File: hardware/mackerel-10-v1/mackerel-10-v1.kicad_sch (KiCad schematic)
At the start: 8 parts, among them J1 Conn_02x05_Odd_Even, U1 68010D, X1 40 MHz

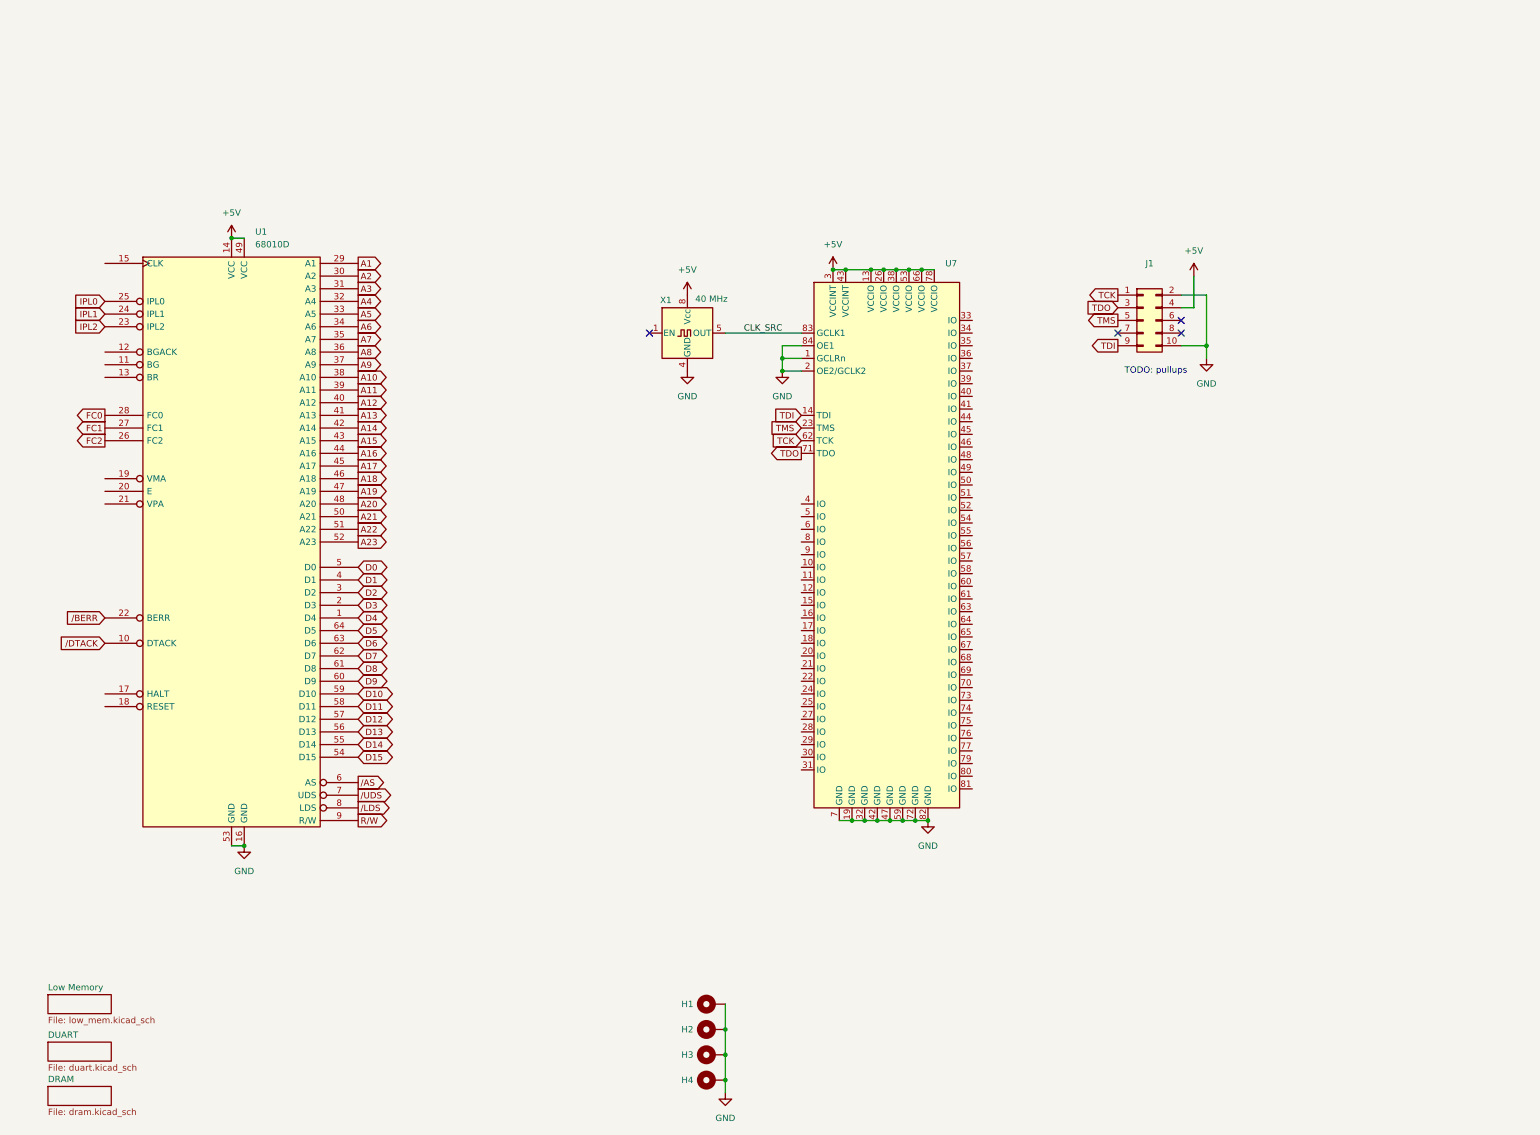
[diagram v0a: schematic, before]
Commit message: Symbol and footprint for SIMM-30 DRAM stubbed out
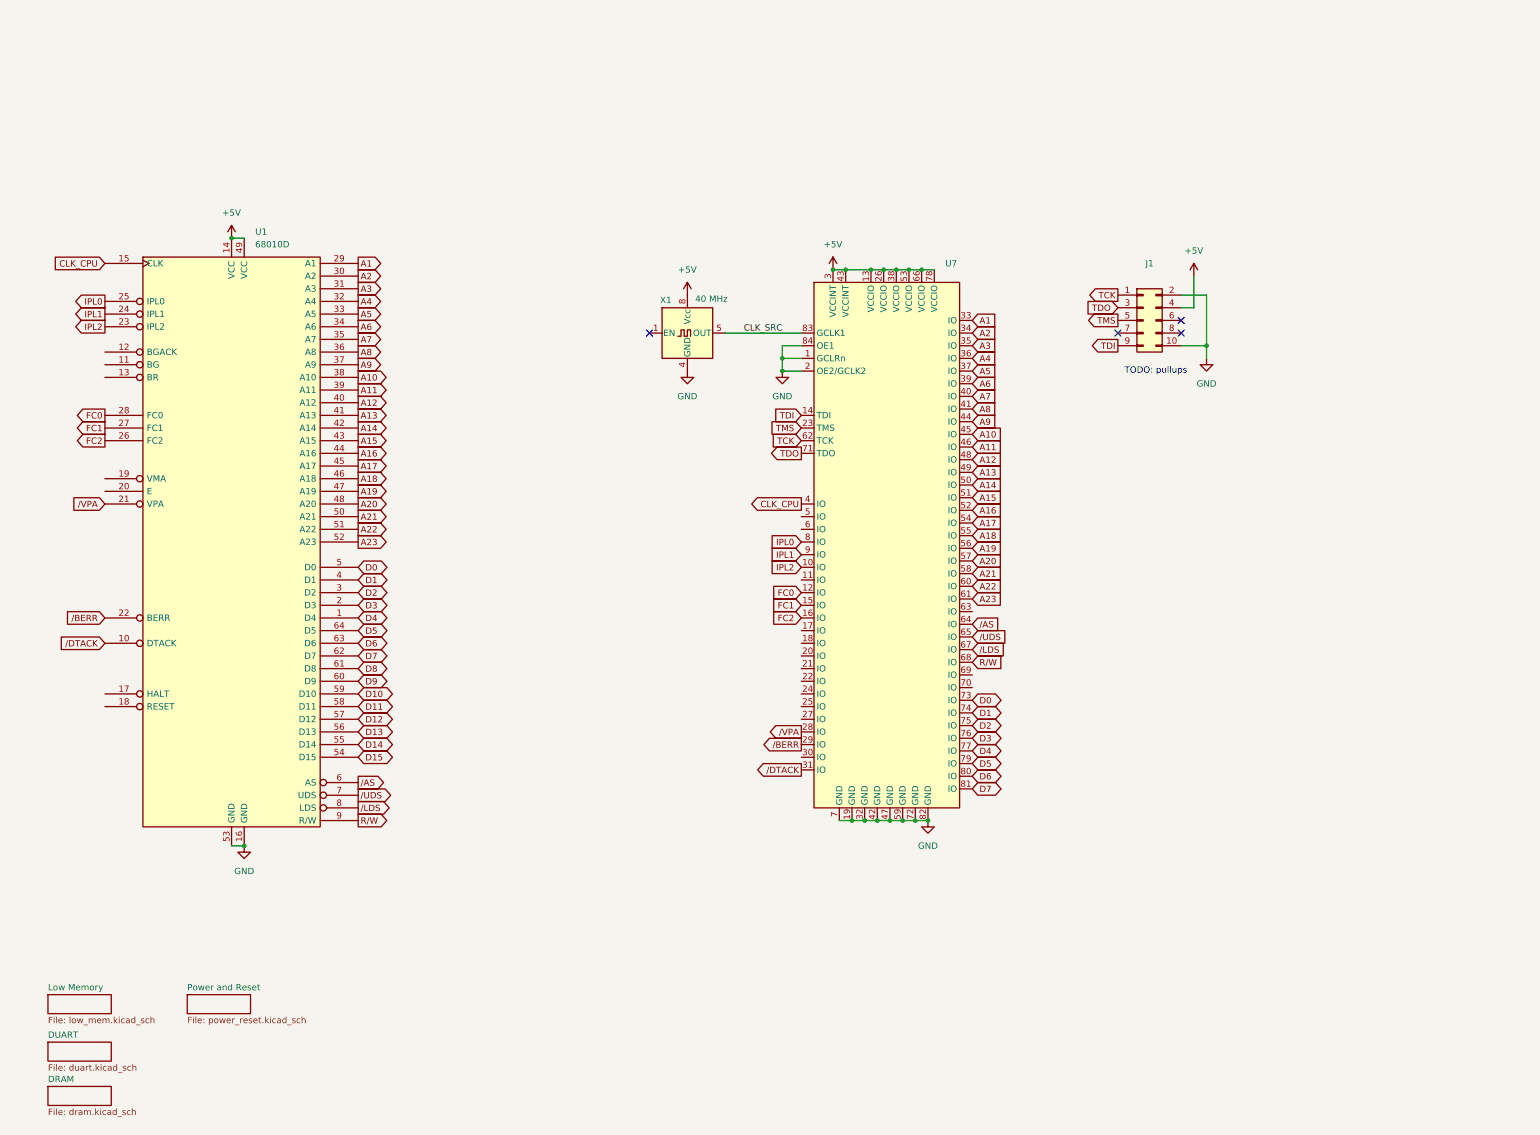
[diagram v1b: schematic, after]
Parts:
- removed H1, H2, H3, H4: MountingHole_Pad, MountingHole:MountingHole_3.2mm_M3_Pad_Via, symbol Mechanical:MountingHole_Pad
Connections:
- net A1: now also U7.33 (IO)
- net A10: now also U7.45 (IO)
- net A11: now also U7.46 (IO)
- net A12: now also U7.48 (IO)
- net A13: now also U7.49 (IO)
- net A14: now also U7.50 (IO)
- net A15: now also U7.51 (IO)
- net A16: now also U7.52 (IO)
- net A17: now also U7.54 (IO)
- net A18: now also U7.55 (IO)
- net A19: now also U7.56 (IO)
- net A2: now also U7.34 (IO)
- net A20: now also U7.57 (IO)
- net A21: now also U7.58 (IO)
- net A22: now also U7.60 (IO)
- net A23: now also U7.61 (IO)
- net A3: now also U7.35 (IO)
- net A4: now also U7.36 (IO)
- net A5: now also U7.37 (IO)
- net A6: now also U7.39 (IO)
- net A7: now also U7.40 (IO)
- net A8: now also U7.41 (IO)
- net A9: now also U7.44 (IO)
- net D0: now also U7.73 (IO)
- net D1: now also U7.74 (IO)
- net D2: now also U7.75 (IO)
- net D3: now also U7.76 (IO)
- net D4: now also U7.77 (IO)
- net D5: now also U7.79 (IO)
- net D6: now also U7.80 (IO)
- net D7: now also U7.81 (IO)
- net FC0: now also U7.12 (IO)
- net FC1: now also U7.15 (IO)
- net FC2: now also U7.16 (IO)
- net IPL0: now also U7.8 (IO)
- net IPL1: now also U7.9 (IO)
- net IPL2: now also U7.10 (IO)
- net R/W: now also U7.68 (IO)
- net /AS: now also U7.64 (IO)
- net /BERR: now also U7.29 (IO)
- net /DTACK: now also U7.31 (IO)
- net /LDS: now also U7.67 (IO)
- net /UDS: now also U7.65 (IO)
- net CLK_CPU: now reaches U1.15 (CLK)
- net CLK_CPU: now also U7.4 (IO)
- net /VPA: now reaches U1.21 (VPA)
- net /VPA: now also U7.28 (IO)
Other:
- added sheet Power and Reset (power_reset.kicad_sch)

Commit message: Trying to figure out Mackerel-10 components
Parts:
- added J2: DIN41612_02x32_AC, Connector_DIN:DIN41612_C_2x32_Male_Horizontal_THT, symbol Connector:DIN41612_02x32_AC
- added R1, R2, R3, R4, R5, R6, R7, R8, R9: R, Resistor_THT:R_Axial_DIN0204_L3.6mm_D1.6mm_P5.08mm_Horizontal, symbol Device:R
- X1: value 40 MHz -> 50 MHz
- renumbered U7 to U2
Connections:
- net +5V: now also R1.1, R2.1, R3.1, R4.1, R5.1, R6.1, R7.1, R8.1
- net A1: no longer U2.33 (IO)
- net A10: no longer U2.45 (IO)
- net A11: no longer U2.46 (IO)
- net A12: no longer U2.48 (IO)
- net A13: no longer U2.49 (IO)
- net A14: no longer U2.50 (IO)
- net A15: no longer U2.51 (IO)
- net A16: now also U2.33 (IO); no longer U2.52 (IO)
- net A17: now also U2.34 (IO); no longer U2.54 (IO)
- net A18: now also U2.35 (IO); no longer U2.55 (IO)
- net A19: now also U2.36 (IO); no longer U2.56 (IO)
- net A2: no longer U2.34 (IO)
- net A20: now also U2.37 (IO); no longer U2.57 (IO)
- net A21: now also U2.39 (IO); no longer U2.58 (IO)
- net A22: now also U2.40 (IO); no longer U2.60 (IO)
- net A23: now also U2.41 (IO); no longer U2.61 (IO)
- net A3: no longer U2.35 (IO)
- net A4: no longer U2.36 (IO)
- net A5: no longer U2.37 (IO)
- net A6: no longer U2.39 (IO)
- net A7: no longer U2.40 (IO)
- net A8: no longer U2.41 (IO)
- net A9: no longer U2.44 (IO)
- net D0: no longer U2.73 (IO)
- net D1: no longer U2.74 (IO)
- net D2: no longer U2.75 (IO)
- net D3: no longer U2.76 (IO)
- net D4: no longer U2.77 (IO)
- net D5: no longer U2.79 (IO)
- net D6: no longer U2.80 (IO)
- net D7: no longer U2.81 (IO)
- net FC0: now also U2.25 (IO); no longer U2.12 (IO)
- net FC1: now also U2.27 (IO); no longer U2.15 (IO)
- net FC2: now also U2.28 (IO); no longer U2.16 (IO)
- net GND: now also R9.2; no longer U2.2 (OE2/GCLK2)
- net IPL0: now also R5.2; no longer U2.8 (IO)
- net IPL1: now also R4.2; no longer U2.9 (IO)
- net IPL2: now also R3.2; no longer U2.10 (IO)
- net R/W: now also U2.77 (IO); no longer U2.68 (IO)
- net TCK: now also R9.1
- net TDI: now also R8.2
- net TDO: now also R6.2
- net TMS: now also R7.2
- net /AS: now also U2.74 (IO); no longer U2.64 (IO)
- net /BERR: now also U2.30 (IO); no longer U2.29 (IO)
- net /LDS: now also U2.76 (IO); no longer U2.67 (IO)
- net /UDS: now also U2.75 (IO); no longer U2.65 (IO)
- net /VPA: now also U2.29 (IO); no longer U2.28 (IO)
- net at U1.12 (BGACK): now also R2.2
- net at U1.13 (BR): now also R1.2
- net /RESET: now reaches U1.17 (HALT)
- net /RESET: now also U1.18 (RESET), U2.5 (IO)
- net /DUART: now reaches U2.11 (IO)
- net /IRQ1: now reaches U2.17 (IO)
- net /IRQ2: now reaches U2.18 (IO)
- net /IRQ3: now reaches U2.20 (IO)
- net /IACK1: now reaches U2.21 (IO)
- net /IACK2: now reaches U2.22 (IO)
- net /IACK3: now reaches U2.24 (IO)
- net /EVENRAM: now reaches U2.6 (IO)
- new net /DTACK_DUART: U2.15 (IO)
- new net /DTACK_EXP: U2.16 (IO)
- new net /EVENROM: U2.9 (IO)
- new net /EXP: U2.12 (IO)
- new net /IPL0: U2.79 (IO)
- new net /IPL1: U2.80 (IO)
- new net /IPL2: U2.81 (IO)
- new net /ODDRAM: U2.8 (IO)
- new net /ODDROM: U2.10 (IO)
- no-connect marks 4 -> 7
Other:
- removed sheet DRAM
- note added: "TODO: IDE lines"
- note added: "TODO: switch to a 44 pin CPLD?"
- note removed: "TODO: pullups"
- moved on the sheet: J1, U1, U2, X1

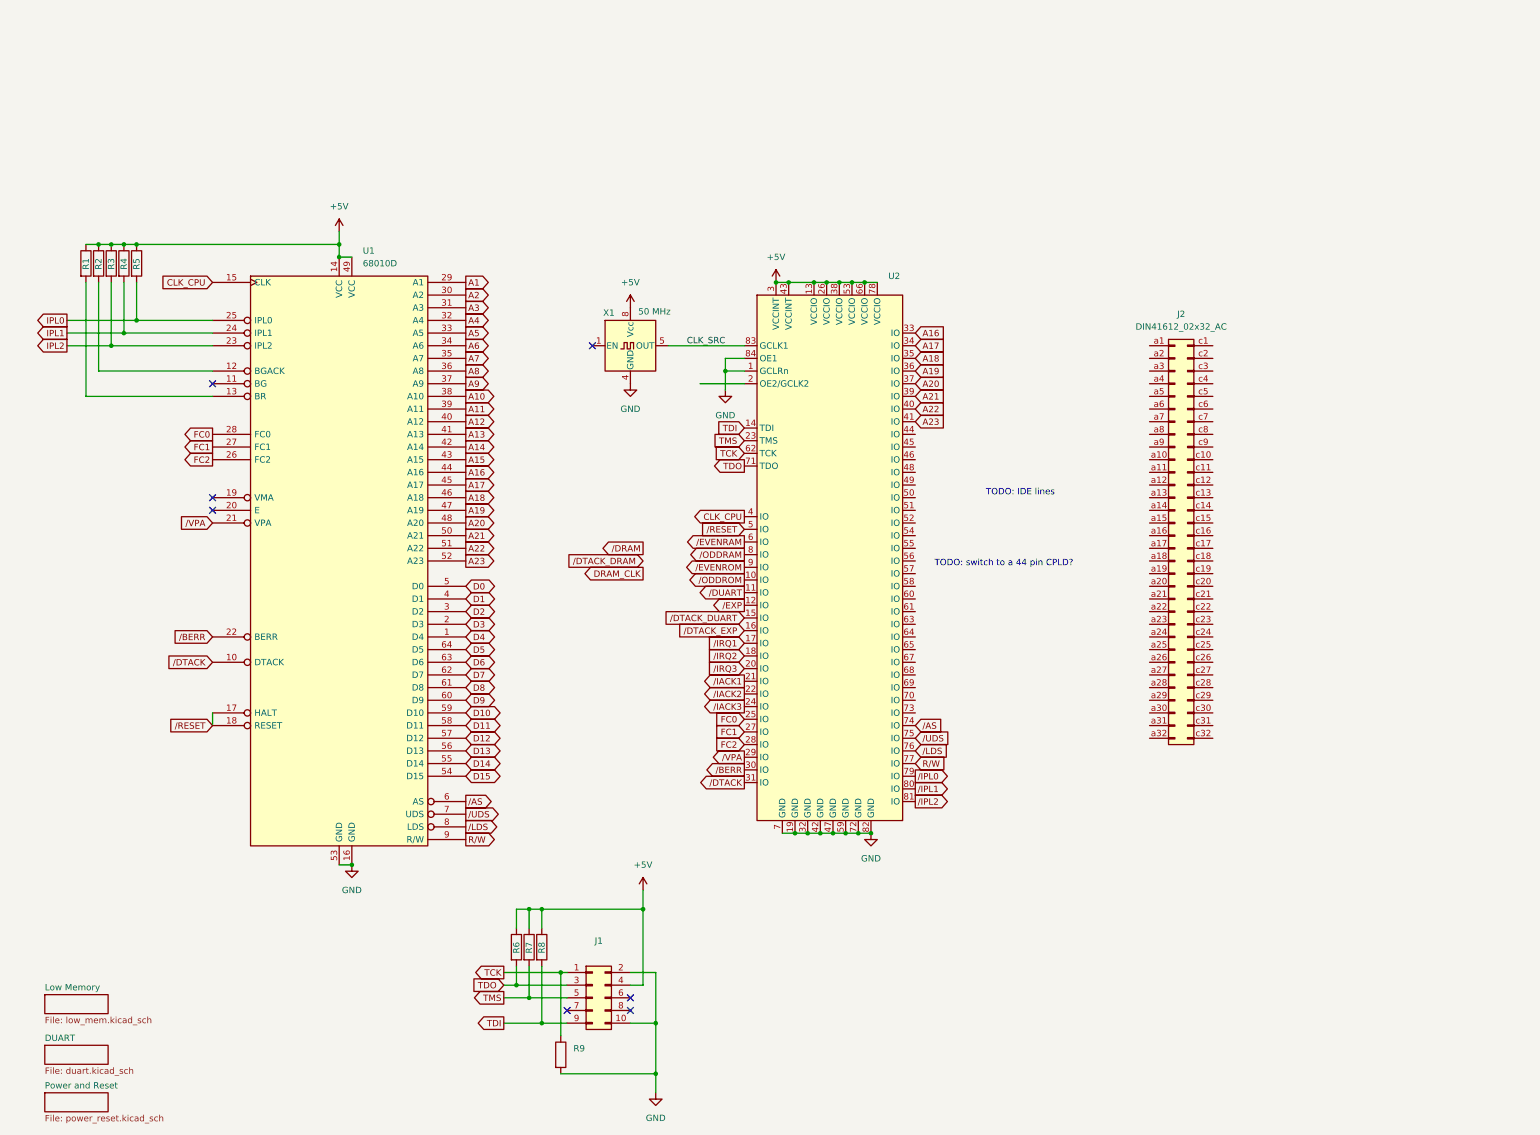
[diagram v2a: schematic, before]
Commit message: More progress on Mackerel-10 schematic and PCB
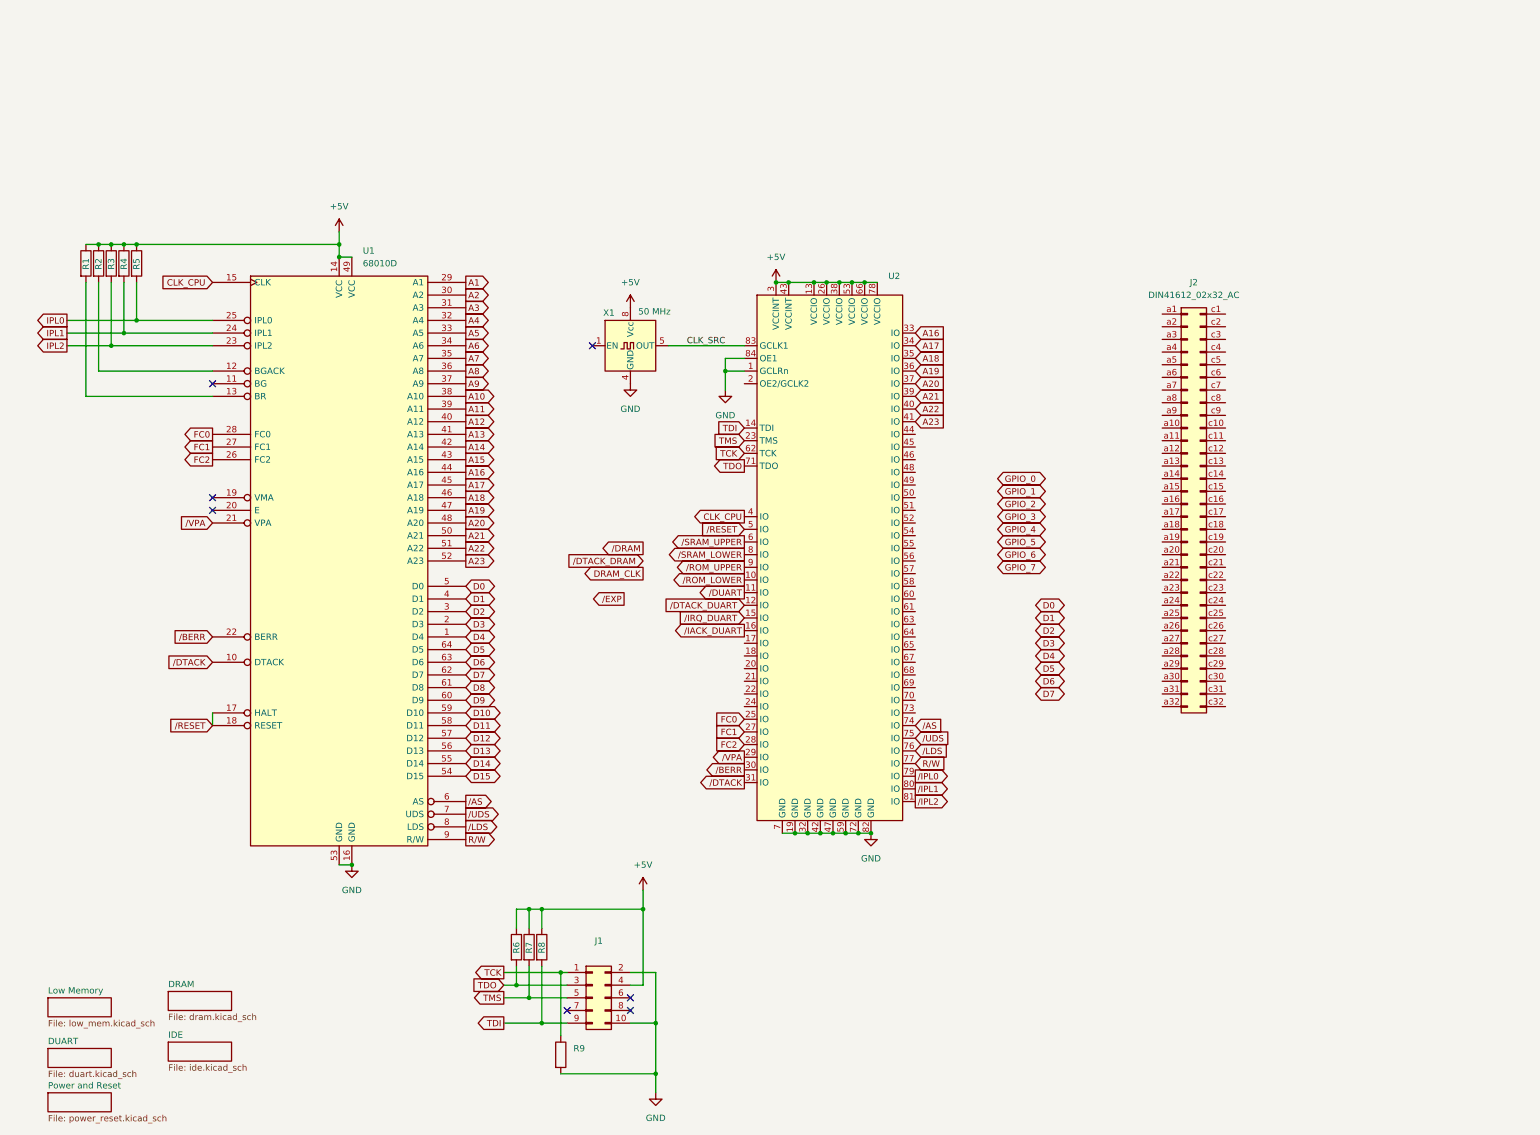
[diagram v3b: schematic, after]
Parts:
- J2: footprint Connector_DIN:DIN41612_C_2x32_Male_Horizontal_THT -> Connector_DIN:DIN41612_C_2x32_Female_Vertical_THT
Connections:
- net /DTACK_DUART: now also U2.12 (IO); no longer U2.15 (IO)
- net /EXP: no longer U2.12 (IO)
- net /DTACK_EXP renamed /IACK_DUART
- net /EVENRAM renamed /SRAM_UPPER
- net /EVENROM renamed /ROM_UPPER
- net /IACK1: no longer names the net of U2.21 (IO)
- net /IACK2: no longer names the net of U2.22 (IO)
- net /IACK3: no longer names the net of U2.24 (IO)
- net /IRQ1: no longer names the net of U2.17 (IO)
- net /IRQ2: no longer names the net of U2.18 (IO)
- net /IRQ3: no longer names the net of U2.20 (IO)
- net /ODDRAM renamed /SRAM_LOWER
- net /ODDROM renamed /ROM_LOWER
- new net /IRQ_DUART: U2.15 (IO)
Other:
- added sheet DRAM (dram.kicad_sch)
- added sheet IDE (ide.kicad_sch)
- note removed: "TODO: IDE lines"
- note removed: "TODO: switch to a 44 pin CPLD?"
